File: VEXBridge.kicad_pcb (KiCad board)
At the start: 2 copper layers, 30 x 40 mm, 37 parts, among them J1 4P4C, J3 Conn_01x05_Pin, U1 LM2596S-5, U2 MAX481E, U5 SN74LVC2G14DBV

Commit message: VEXBridge v2 (WIP)
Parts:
- removed D4: ESDA5V3L, Package_TO_SOT_SMD:SOT-23-3
- removed U1: LM2596S-5, Package_TO_SOT_SMD:TO-263-5_TabPin3
- removed kibuzzard-675F6148: G***, kibuzzard-675F6148
- removed kibuzzard-675F61D9: G***, kibuzzard-675F61D9
- removed kibuzzard-675F61E2: G***, kibuzzard-675F61E2
- removed kibuzzard-675F61ED: G***, kibuzzard-675F61ED
- removed kibuzzard-675F6473: G***, kibuzzard-675F6473
- removed kibuzzard-675F648F: G***, kibuzzard-675F648F
- removed kibuzzard-675F6495: G***, kibuzzard-675F6495
- removed kibuzzard-676E54E7: G***, kibuzzard-676E54E7
- added C6: 10uF, Capacitor_SMD:C_0201_0603Metric, F.Cu at (81.0, 54.5)
- added C7: 22uF, Capacitor_SMD:C_1206_3216Metric, F.Cu at (81.0, 52.0)
- added C8: 1uF, Capacitor_SMD:C_0201_0603Metric, F.Cu at (63.3, 80.0)
- added F1: 1A, Fuse:Fuse_2010_5025Metric, F.Cu at (65.2, 43.0)
- added J10: QWIIC Connector, Connector_JST:JST_SH_SM04B-SRSS-TB_1x04-1MP_P1.00mm_Horizontal, F.Cu at (53.5, 37.5)
- added J2: Conn_01x04, Connector_Molex:Molex_PicoBlade_53047-0410_1x04_P1.25mm_Vertical, F.Cu at (91.3, 35.5)
- added J4: QWIIC Connector, Connector_JST:JST_SH_SM04B-SRSS-TB_1x04-1MP_P1.00mm_Horizontal, F.Cu at (53.5, 53.1)
- added J5: QWIIC Connector, Connector_JST:JST_SH_SM04B-SRSS-TB_1x04-1MP_P1.00mm_Horizontal, F.Cu at (53.5, 60.9)
- added J6: Conn_01x04, Connector_Molex:Molex_PicoBlade_53047-0410_1x04_P1.25mm_Vertical, F.Cu at (91.3, 51.0)
- added J7: Conn_01x04, Connector_Molex:Molex_PicoBlade_53047-0410_1x04_P1.25mm_Vertical, F.Cu at (91.3, 58.8)
- added J8: USB_C_Receptacle_USB2.0_14P, Connector_USB:USB_C_Plug_Molex_105444, F.Cu at (80.8, 26.6)
- added J9: QWIIC Connector, Connector_JST:JST_SH_SM04B-SRSS-TB_1x04-1MP_P1.00mm_Horizontal, F.Cu at (53.5, 45.3)
- added R10: 10k, Resistor_SMD:R_0805_2012Metric, F.Cu at (58.5, 39.0)
- added R11: 5.1k, Resistor_SMD:R_0805_2012Metric, F.Cu at (92.1, 76.2)
- added R13: 5.1k, Resistor_SMD:R_0805_2012Metric, F.Cu at (82.0, 30.5)
- added R14: 5.1k, Resistor_SMD:R_0805_2012Metric, F.Cu at (82.0, 32.5)
- added U3: LSM9DS1, Package_LGA:LGA-24L_3x3.5mm_P0.43mm, F.Cu at (58.4, 76.1)
- added U4: AMS1117-3.3, Package_TO_SOT_SMD:SOT-223-3_TabPin2, F.Cu at (81.0, 60.0)
- C1: value 100uF -> 220uF; footprint Capacitor_SMD:CP_Elec_6.3x7.7 -> Capacitor_SMD:C_1210_3225Metric
- C2: value 220uF -> 100uF; footprint Capacitor_SMD:CP_Elec_6.3x7.7 -> Capacitor_SMD:C_1206_3216Metric
- C3, C4: value 0.1uF -> 1uF; footprint Capacitor_SMD:C_0402_1005Metric -> Capacitor_SMD:C_0201_0603Metric
- D1: value LED -> RED
- D2: value LED -> GREEN
- D3: value LED -> D; footprint LED_SMD:LED_0603_1608Metric -> Diode_SMD:D_0201_0603Metric
- J3: value Conn_01x05_Pin -> Conn_01x04; footprint Connector_PinHeader_2.54mm:PinHeader_1x05_P2.54mm_Vertical -> Connector_Molex:Molex_PicoBlade_53047-0410_1x04_P1.25mm_Vertical
- L1: value 47uH -> 68uH; footprint Inductor_SMD:L_Coilcraft_LPS4018 -> Inductor_SMD:L_SXN_SMDRI127
- R1: value 100 -> 5.1k
- R2: value 120 -> 10k; footprint Resistor_SMD:R_1206_3216Metric -> Resistor_SMD:R_0805_2012Metric
- R3, R4: value 100 -> 10k
- U2: value MAX481E -> ESP32-S3-MINI-1U; footprint Package_SO:SOIC-8_3.9x4.9mm_P1.27mm -> RF_Module:ESP32-S2-MINI-1U
- U5: value SN74LVC2G14DBV -> LM2595S-5; footprint Package_TO_SOT_SMD:SOT-23-6 -> Package_TO_SOT_SMD:TO-263-5_TabPin3
- moved H1 83.5 mm to (55.0, 30.0)
- moved R6 73.0 mm to (58.5, 37.0), turned to 180 degrees
- moved H3 62.4 mm to (55.0, 85.0)
- moved D3 59.7 mm to (81.8, 34.5), turned to 180 degrees
- moved L1 56.9 mm to (32.0, 53.5)
- moved R5 56.2 mm to (58.5, 63.0)
- moved J1 54.8 mm to (70.3, 36.5), turned to 180 degrees
- moved R2 49.5 mm to (62.0, 81.5)
- moved C2 48.2 mm to (66.0, 47.0)
- moved R7 47.6 mm to (58.5, 45.0), turned to 180 degrees
- moved R3 47.4 mm to (58.5, 53.0), turned to 180 degrees
- moved C1 47.3 mm to (71.0, 47.0), turned to 180 degrees
- moved R8 44.8 mm to (58.5, 47.0), turned to 180 degrees
- moved R4 43.6 mm to (58.5, 61.0), turned to 180 degrees
- moved R9 38.5 mm to (58.5, 55.1), turned to 180 degrees
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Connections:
- C3 pad 1: +5V -> +3.3V
- C4 pad 1: +5V -> +3.3V
- D3 pad 1: GND -> +5V
- J1 pad 1: A -> unconnected-(J1-Pad1)
- J1 pad 2: B -> unconnected-(J1-Pad2)
- J1 pad 4: +12V -> Net-(F1-Pad1)
- J3 pad 1: RTS -> +5V
- J3 pad 2: RXD -> ENC_A1
- J3 pad 3: TXD -> ENC_B1
- R1 pad 1: +5V -> Net-(D1-A)
- R1 pad 2: Net-(D1-A) -> +3.3V
- R2 pad 1: B -> +3.3V
- R2 pad 2: A -> Net-(U2-EN)
- R3 pad 1: Net-(U5-1Y) -> +3.3V
- R3 pad 2: Net-(D2-A) -> SDA
- R4 pad 1: Net-(U5-2Y) -> +3.3V
- R4 pad 2: Net-(D3-A) -> SDA
- R5 pad 1: B -> +3.3V
- R5 pad 2: GND -> SCL
- R6 pad 1: +5V -> +3.3V
- R6 pad 2: A -> SDA
- R7 pad 1: +5V -> +3.3V
- R7 pad 2: TXD -> SDA
- R8 pad 1: RTS -> +3.3V
- R8 pad 2: GND -> SCL
- R9 pad 1: +5V -> +3.3V
- R9 pad 2: RXD -> SCL
- U2 pad 1: TXD -> GND
- U2 pad 2: RTS -> GND
- U2 pad 3: RTS -> +3.3V
- U2 pad 4: RXD -> SDA
- U2 pad 5: GND -> SCL
- U2 pad 6: A -> unconnected-(U2-IO2-Pad6)
- U2 pad 7: B -> unconnected-(U2-IO3-Pad7)
- U2 pad 8: +5V -> ENC_A1
- U5 pad 1: RXD -> Net-(D9-K)
- U5 pad 2: GND -> +12V
- U5 pad 3: TXD -> GND
- U5 pad 4: Net-(U5-2Y) -> +5V
- U5 pad 5: +5V -> GND
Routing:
- net +5V: track 91.8 -> 0.00 mm, vias 4 -> 0
- net GND: track 52.9 -> 0.00 mm, vias 7 -> 0
- net A: track 31.0 -> 0.00 mm, vias 2 -> 0
- net B: track 25.0 -> 0.00 mm
- net TXD: track 23.8 -> 0.00 mm, vias 3 -> 0
- net +12V: track 20.6 -> 0.00 mm
- net RXD: track 15.0 -> 0.00 mm, vias 1 -> 0
- net RTS: track 14.1 -> 0.00 mm, vias 1 -> 0
- net Net-(D9-K): track 12.2 -> 0.00 mm
- net Net-(U5-2Y): track 6.82 -> 0.00 mm
- net Net-(D2-A): track 4.65 -> 0.00 mm
- net Net-(D3-A): track 4.49 -> 0.00 mm
- net Net-(D1-A): track 4.34 -> 0.00 mm
- net Net-(U5-1Y): track 2.13 -> 0.00 mm
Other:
- board size 30 x 40 mm -> 45 x 65 mm

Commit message: Completed schematic
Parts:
- removed C1: 220uF, Capacitor_SMD:C_1210_3225Metric
- removed C2: 100uF, Capacitor_SMD:C_1206_3216Metric
- removed C3, C4, C8: 1uF, Capacitor_SMD:C_0201_0603Metric
- removed C6: 10uF, Capacitor_SMD:C_0201_0603Metric
- removed C7: 22uF, Capacitor_SMD:C_1206_3216Metric
- removed D1: RED, LED_SMD:LED_0603_1608Metric
- removed D2: GREEN, LED_SMD:LED_0603_1608Metric
- removed D3: D, Diode_SMD:D_0201_0603Metric
- removed D9: D_Schottky, Diode_SMD:D_SMA
- removed F1: 1A, Fuse:Fuse_2010_5025Metric
- removed G***: LOGO, LOGO
- removed H1, H2, H3, H4: MountingHole_Pad, MountingHole:MountingHole_2.7mm_M2.5_Pad
- removed J1: 4P4C, Connector_RJ:RJ9_Evercom_5301-440xxx_Horizontal
- removed J10, J4, J5, J9: QWIIC Connector, Connector_JST:JST_SH_SM04B-SRSS-TB_1x04-1MP_P1.00mm_Horizontal
- removed J2, J3, J6, J7: Conn_01x04, Connector_Molex:Molex_PicoBlade_53047-0410_1x04_P1.25mm_Vertical
- removed J8: USB_C_Receptacle_USB2.0_14P, Connector_USB:USB_C_Plug_Molex_105444
- removed L1: 68uH, Inductor_SMD:L_SXN_SMDRI127
- removed R1, R11, R13, R14: 5.1k, Resistor_SMD:R_0805_2012Metric
- removed R10, R2, R3, R4, R5, R6, R7, R8, R9: 10k, Resistor_SMD:R_0805_2012Metric
- removed U2: ESP32-S3-MINI-1U, RF_Module:ESP32-S2-MINI-1U
- removed U3: LSM9DS1, Package_LGA:LGA-24L_3x3.5mm_P0.43mm
- removed U4: AMS1117-3.3, Package_TO_SOT_SMD:SOT-223-3_TabPin2
- removed U5: LM2595S-5, Package_TO_SOT_SMD:TO-263-5_TabPin3
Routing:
- removed copper zone on B.Cu, net GND
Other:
- board outline removed

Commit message: Initial PCB Design w/o power rails
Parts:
- added C1: 0.1uF, Capacitor_SMD:C_0603_1608Metric, F.Cu at (131.3, 50.8)
- added C10: 1uF, Capacitor_SMD:C_0603_1608Metric, F.Cu at (131.2, 52.5)
- added C11: 1uF, Capacitor_SMD:C_0603_1608Metric, F.Cu at (104.0, 43.0)
- added C12: 4.7uF, Capacitor_SMD:C_0603_1608Metric, F.Cu at (80.5, 39.7)
- added C13: 1uF, Capacitor_SMD:C_0603_1608Metric, F.Cu at (117.0, 63.0)
- added C14: 22uF, Capacitor_SMD:C_0603_1608Metric, F.Cu at (79.0, 39.7)
- added C15: 1uF, Capacitor_SMD:C_0603_1608Metric, F.Cu at (99.0, 36.5)
- added C2: 10uF, Capacitor_SMD:C_0603_1608Metric, F.Cu at (120.5, 52.5)
- added C3: 220nF, Capacitor_SMD:C_0402_1005Metric, F.Cu at (119.0, 53.0)
- added C4: 22uF, Capacitor_SMD:C_0603_1608Metric, F.Cu at (136.5, 48.0)
- added C5: 22uF, Capacitor_SMD:C_0603_1608Metric, F.Cu at (136.5, 49.5)
- added C6: 22uF, Capacitor_SMD:C_0603_1608Metric, F.Cu at (136.5, 51.0)
- added C7: 22uF, Capacitor_SMD:C_0603_1608Metric, F.Cu at (136.5, 52.5)
- added C8: 10uF, Capacitor_SMD:C_0603_1608Metric, F.Cu at (139.3, 43.3)
- added C9: 22uF, Capacitor_SMD:C_0603_1608Metric, F.Cu at (139.3, 37.5)
- added D1: D, Diode_SMD:D_0201_0603Metric, F.Cu at (133.5, 47.5)
- added D2: D, Diode_SMD:D_0201_0603Metric, F.Cu at (136.5, 26.5)
- added D3: RED, LED_SMD:LED_0603_1608Metric, F.Cu at (93.0, 60.0)
- added D4: BLUE, LED_SMD:LED_0603_1608Metric, F.Cu at (86.5, 60.0)
- added F1: 2A, Fuse:Fuse_2010_5025Metric, F.Cu at (119.5, 57.5)
- added H1: MountingHole_Pad, MountingHole:MountingHole_2.7mm_M2.5_Pad, F.Cu at (137.5, 19.5)
- added H2: MountingHole_Pad, MountingHole:MountingHole_2.7mm_M2.5_Pad, F.Cu at (137.5, 71.0)
- added H3: MountingHole_Pad, MountingHole:MountingHole_2.7mm_M2.5_Pad, F.Cu at (42.0, 19.5)
- added H4: MountingHole_Pad, MountingHole:MountingHole_2.7mm_M2.5_Pad, F.Cu at (42.0, 71.0)
- added J1: VEX V5, Connector_RJ:RJ9_Evercom_5301-440xxx_Horizontal, F.Cu at (125.7, 63.6)
- added J10: Port 1, Connector_Molex:Molex_Mini-Fit_Jr_5569-04A2_2x02_P4.20mm_Horizontal, F.Cu at (53.5, 30.3)
- added J11: Port 2, Connector_Molex:Molex_Mini-Fit_Jr_5569-04A2_2x02_P4.20mm_Horizontal, F.Cu at (53.5, 41.7)
- added J12: Port 3, Connector_Molex:Molex_Mini-Fit_Jr_5569-04A2_2x02_P4.20mm_Horizontal, F.Cu at (53.5, 53.2)
- added J13: Port 4, Connector_Molex:Molex_Mini-Fit_Jr_5569-04A2_2x02_P4.20mm_Horizontal, F.Cu at (53.5, 64.7)
- added J14: USB_C_Receptacle_USB2.0_14P, Connector_USB:USB_C_Plug_Molex_105444, F.Cu at (139.0, 28.2)
- added J2: Port A, Connector_JST:JST_SH_SM04B-SRSS-TB_1x04-1MP_P1.00mm_Horizontal, F.Cu at (74.8, 70.1)
- added J3: Port B, Connector_JST:JST_SH_SM04B-SRSS-TB_1x04-1MP_P1.00mm_Horizontal, F.Cu at (83.3, 70.1)
- added J4: Port C, Connector_JST:JST_SH_SM04B-SRSS-TB_1x04-1MP_P1.00mm_Horizontal, F.Cu at (91.8, 70.1)
- added J5: Port D, Connector_JST:JST_SH_SM04B-SRSS-TB_1x04-1MP_P1.00mm_Horizontal, F.Cu at (100.3, 70.1)
- added J6: Port E, Connector_JST:JST_SH_SM04B-SRSS-TB_1x04-1MP_P1.00mm_Horizontal, F.Cu at (99.8, 20.4)
- added J7: Port F, Connector_JST:JST_SH_SM04B-SRSS-TB_1x04-1MP_P1.00mm_Horizontal, F.Cu at (91.3, 20.5)
- added J8: Port G, Connector_JST:JST_SH_SM04B-SRSS-TB_1x04-1MP_P1.00mm_Horizontal, F.Cu at (82.8, 20.5)
- added J9: Port H, Connector_JST:JST_SH_SM04B-SRSS-TB_1x04-1MP_P1.00mm_Horizontal, F.Cu at (74.3, 20.5)
- added JP2: Multiplexer Addr, Jumper:SolderJumper-3_P1.3mm_Bridged12_RoundedPad1.0x1.5mm, F.Cu at (101.0, 40.3)
- added L1: 10uH, Inductor_SMD:L_0603_1608Metric, F.Cu at (134.0, 50.3)
- added Q1: BSS138, Package_TO_SOT_SMD:SOT-23-3, F.Cu at (65.9, 31.0)
- added Q2: BSS138, Package_TO_SOT_SMD:SOT-23-3, F.Cu at (66.1, 42.0)
- added Q3: BSS138, Package_TO_SOT_SMD:SOT-23-3, F.Cu at (66.1, 53.5)
- added Q4: BSS138, Package_TO_SOT_SMD:SOT-23-3, F.Cu at (66.0, 65.4)
- added Q5: BSS138, Package_TO_SOT_SMD:SOT-23-3, F.Cu at (65.9, 26.0)
- added Q6: BSS138, Package_TO_SOT_SMD:SOT-23-3, F.Cu at (66.1, 37.0)
- added Q7: BSS138, Package_TO_SOT_SMD:SOT-23-3, F.Cu at (66.1, 48.5)
- added Q8: BSS138, Package_TO_SOT_SMD:SOT-23-3, F.Cu at (66.0, 59.5)
- added R1: 100k, Resistor_SMD:R_0805_2012Metric, F.Cu at (131.6, 54.5)
- added R10: 10k, Resistor_SMD:R_0805_2012Metric, F.Cu at (69.1, 42.0)
- added R11: 10k, Resistor_SMD:R_0805_2012Metric, F.Cu at (63.1, 40.5)
- added R12: 10k, Resistor_SMD:R_0805_2012Metric, F.Cu at (69.1, 53.5)
- added R13: 10k, Resistor_SMD:R_0805_2012Metric, F.Cu at (63.1, 52.0)
- added R14: 10k, Resistor_SMD:R_0805_2012Metric, F.Cu at (69.0, 65.6)
- added R15: 10k, Resistor_SMD:R_0805_2012Metric, F.Cu at (63.1, 63.5)
- added R16: 10k, Resistor_SMD:R_0805_2012Metric, F.Cu at (69.0, 26.0)
- added R17: 10k, Resistor_SMD:R_0805_2012Metric, F.Cu at (63.1, 27.5)
- added R18: 10k, Resistor_SMD:R_0805_2012Metric, F.Cu at (69.1, 36.9)
- added R19: 10k, Resistor_SMD:R_0805_2012Metric, F.Cu at (63.1, 38.5)
- added R2: 24k, Resistor_SMD:R_0805_2012Metric, F.Cu at (135.1, 54.5)
- added R20: 10k, Resistor_SMD:R_0805_2012Metric, F.Cu at (69.1, 48.5)
- added R21: 10k, Resistor_SMD:R_0805_2012Metric, F.Cu at (63.1, 50.0)
- added R22: 10k, Resistor_SMD:R_0805_2012Metric, F.Cu at (69.0, 59.5)
- added R23: 10k, Resistor_SMD:R_0805_2012Metric, F.Cu at (63.1, 61.5)
- added R24: 5.1k, Resistor_SMD:R_0805_2012Metric, F.Cu at (133.0, 25.5)
- added R25: 5.1k, Resistor_SMD:R_0805_2012Metric, F.Cu at (135.0, 25.5)
- added R26: 4.7k, Resistor_SMD:R_0805_2012Metric, F.Cu at (91.0, 59.8)
- added R27: 2.2k, Resistor_SMD:R_0805_2012Metric, F.Cu at (88.5, 59.8)
- added R28: 10k, Resistor_SMD:R_0805_2012Metric, F.Cu at (112.5, 70.5)
- added R29: 10k, Resistor_SMD:R_0805_2012Metric, F.Cu at (109.5, 66.5)
- added R3: 2k, Resistor_SMD:R_0805_2012Metric, F.Cu at (80.5, 54.6)
- added R30: 10k, Resistor_SMD:R_0805_2012Metric, F.Cu at (120.0, 68.5)
- added R31: 10k, Resistor_SMD:R_0805_2012Metric, F.Cu at (120.0, 64.5)
- added R32: 900, Resistor_SMD:R_0805_2012Metric, F.Cu at (138.6, 54.5)
- added R4: 2k, Resistor_SMD:R_0805_2012Metric, F.Cu at (78.5, 54.6)
- added R5: 10k, Resistor_SMD:R_0805_2012Metric, F.Cu at (99.4, 34.5)
- added R6: 10K, Resistor_SMD:R_0805_2012Metric, F.Cu at (104.0, 48.0)
- added R7: 10k, Resistor_SMD:R_0805_2012Metric, F.Cu at (113.0, 62.5)
- added R8: 10k, Resistor_SMD:R_0805_2012Metric, F.Cu at (69.0, 31.0)
- added R9: 10k, Resistor_SMD:R_0805_2012Metric, F.Cu at (63.1, 29.5)
- added SW1: Reset, Button_Switch_SMD:SW_SPST_TS-1088-xR020, F.Cu at (94.5, 34.0)
- added SW2: Boot, Button_Switch_SMD:SW_SPST_TS-1088-xR020, F.Cu at (85.0, 34.0)
- added U1: LMR33630ADDA, Package_SO:Texas_HSOP-8-1EP_3.9x4.9mm_P1.27mm_ThermalVias, F.Cu at (125.3, 52.6)
- added U2: AMS1117-3.3, Package_TO_SOT_SMD:SOT-223-3_TabPin2, F.Cu at (134.5, 40.4)
- added U3: D3V3XA4B10LP, Package_DFN_QFN:Diodes_UDFN-10_1x2.5mm_P0.5mm, F.Cu at (135.0, 30.6)
- added U4: PCA9548ADB, Package_SO:SSOP-24_5.3x8.2mm_P0.65mm, F.Cu at (109.4, 45.5)
- added U6: ESP32-S3-MINI-1U, RF_Module:ESP32-S2-MINI-1U, F.Cu at (89.7, 45.4)
- added U7: MAX485E, Package_SO:SOIC-8_3.9x4.9mm_P1.27mm, F.Cu at (115.0, 66.5)
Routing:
- net USB_D-: track 0.00 -> 60.0 mm, vias 0 -> 2
- net USB_D+: track 0.00 -> 58.6 mm, vias 0 -> 2
- net SCL8: track 0.00 -> 51.8 mm
- net SDA1: track 0.00 -> 47.9 mm
- net SCL7: track 0.00 -> 45.4 mm
- net SCL1: track 0.00 -> 44.4 mm
- net SDA8: track 0.00 -> 44.2 mm
- net SDA2: track 0.00 -> 41.4 mm
- net SCL6: track 0.00 -> 39.1 mm
- net TX: track 0.00 -> 38.9 mm, vias 0 -> 2
- net SDA7: track 0.00 -> 38.0 mm
- net SCL2: track 0.00 -> 37.8 mm
- net RTS: track 0.00 -> 35.2 mm, vias 0 -> 2
- net SDA3: track 0.00 -> 35.0 mm
- net SDA: track 0.00 -> 33.4 mm, vias 0 -> 2
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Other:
- board outline added: 103.5 x 59.5 mm

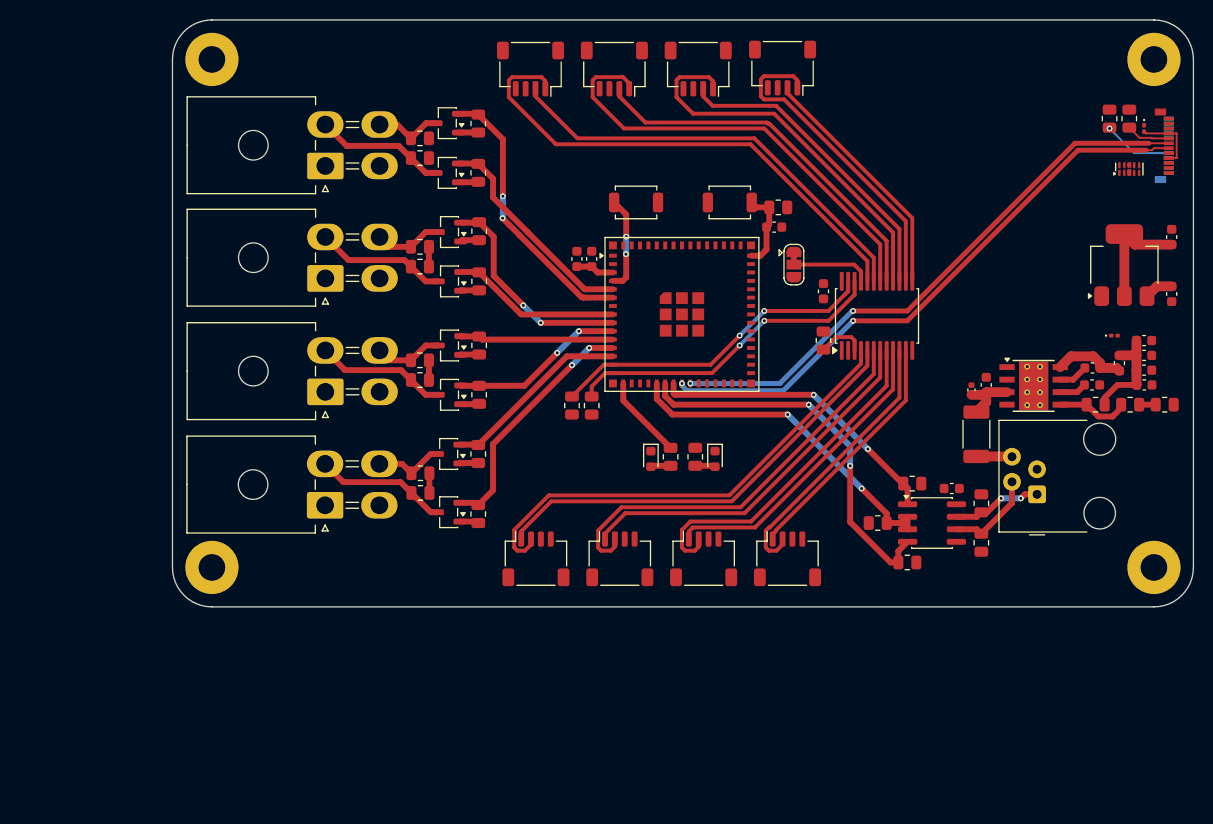
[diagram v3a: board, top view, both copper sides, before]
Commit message: (Mostly) complete PCB routing
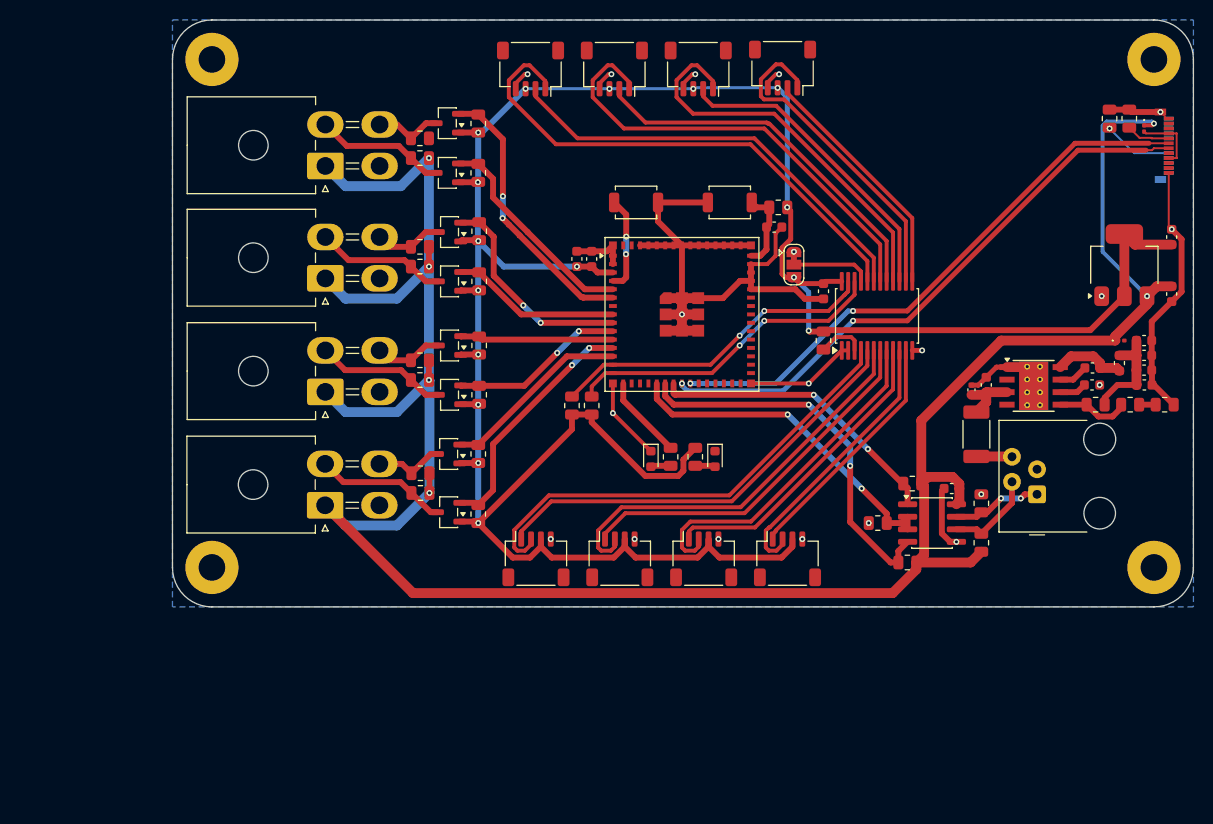
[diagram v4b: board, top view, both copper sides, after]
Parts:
- removed U3: D3V3XA4B10LP, Package_DFN_QFN:Diodes_UDFN-10_1x2.5mm_P0.5mm
- moved D1 0.84 mm to (134.2, 48.0)
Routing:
- net +5V: track 8.91 -> 242.0 mm, vias 0 -> 6
- net +3.3V: track 30.8 -> 252.9 mm, vias 0 -> 16
- net GND: track 0.00 -> 143.2 mm, vias 0 -> 20
- net SCL7: track 45.4 -> 46.5 mm
- net SCL5: track 32.5 -> 33.5 mm
- net SCL6: track 39.1 -> 40.1 mm
- net SCL8: track 51.8 -> 52.8 mm
- added copper zone on B.Cu, net GND

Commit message: Near-Final PCB Design
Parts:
- removed D1, D2: D, Diode_SMD:D_0201_0603Metric
- removed J14: USB_C_Receptacle_USB2.0_14P, Connector_USB:USB_C_Plug_Molex_105444
- removed U4: PCA9548ADB, Package_SO:SSOP-24_5.3x8.2mm_P0.65mm
- added G***: LOGO, LOGO, B.Cu at (114.0, 29.0)
- added J15: USB_C_Receptacle, Connector_USB:USB_C_Receptacle_Molex_105450-0101, F.Cu at (137.1, 29.0)
- added U3: D3V3XA4B10LP, Package_DFN_QFN:Diodes_UDFN-10_1x2.5mm_P0.5mm, F.Cu at (130.5, 26.9)
- added U5: TCA9548APWR, Package_SO:TSSOP-24_4.4x7.8mm_P0.65mm, F.Cu at (109.5, 46.0)
- added kibuzzard-69FA45C9: G***, kibuzzard-69FA45C9, F.Cu at (74.8, 74.0)
- added kibuzzard-69FA4619: G***, kibuzzard-69FA4619, F.Cu at (83.2, 74.0)
- added kibuzzard-69FA461D: G***, kibuzzard-69FA461D, F.Cu at (91.8, 74.0)
- added kibuzzard-69FA4621: G***, kibuzzard-69FA4621, F.Cu at (100.4, 74.0)
- added kibuzzard-69FA465C: G***, kibuzzard-69FA465C, F.Cu at (99.8, 16.4)
- added kibuzzard-69FA4660: G***, kibuzzard-69FA4660, F.Cu at (91.4, 16.4)
- added kibuzzard-69FA4664: G***, kibuzzard-69FA4664, F.Cu at (82.8, 16.4)
- added kibuzzard-69FA4669: G***, kibuzzard-69FA4669, F.Cu at (74.4, 16.4)
- added kibuzzard-69FA46AE: G***, kibuzzard-69FA46AE, F.Cu at (38.6, 28.0)
- added kibuzzard-69FA46BE: G***, kibuzzard-69FA46BE, F.Cu at (38.6, 62.6)
- added kibuzzard-69FA46C2: G***, kibuzzard-69FA46C2, F.Cu at (38.6, 51.2)
- added kibuzzard-69FA46C9: G***, kibuzzard-69FA46C9, F.Cu at (38.6, 39.6)
- C14, C4, C5, C6, C7, C9: footprint Capacitor_SMD:C_0603_1608Metric -> Capacitor_SMD:C_0805_2012Metric
- D4: value BLUE -> GREEN
- F1: footprint Fuse:Fuse_2010_5025Metric -> Fuse:Fuse_1812_4532Metric
- L1: footprint Inductor_SMD:L_0603_1608Metric -> Inductor_SMD:L_TechFuse_SL0420
- R26: value 4.7k -> 330
- R27: value 2.2k -> 150
- R32: value 900 -> 820; footprint Resistor_SMD:R_0805_2012Metric -> Resistor_SMD:R_0603_1608Metric
- moved C4 8.93 mm to (138.5, 39.3)
- moved C5 8.44 mm to (138.5, 41.3)
- moved C6 7.96 mm to (138.5, 43.3)
- moved C7 7.45 mm to (138.4, 45.3)
- moved R25 5.85 mm to (129.5, 23.5)
- moved C8 5.31 mm to (134.3, 45.1)
- moved C9 5.31 mm to (134.3, 39.3)
- moved U2 5.31 mm to (129.5, 42.1)
- moved R24 2.50 mm to (131.5, 23.5)
- moved J1 2.00 mm to (127.7, 63.5)
- moved L1 1.51 mm to (135.5, 50.5)
- moved H3 0.60 mm to (41.4, 19.5)
- moved H4 0.60 mm to (41.4, 71.0)
- moved C14 0.50 mm to (78.5, 39.7)
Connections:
- C4 pad 1: Net-(D1-A) -> +5V
- C5 pad 1: Net-(D1-A) -> +5V
- C6 pad 1: Net-(D1-A) -> +5V
- C7 pad 1: Net-(D1-A) -> +5V
- L1 pad 2: Net-(D1-A) -> +5V
- R1 pad 1: Net-(D1-A) -> +5V
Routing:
- net SCL6: track 40.1 -> 28.6 mm
- net SCL7: track 46.5 -> 35.5 mm
- net Net-(D1-A): track 10.8 -> 0.00 mm
- net SCL8: track 52.8 -> 42.5 mm
- net SCL5: track 33.5 -> 25.3 mm
- net Net-(J15-CC1): track 4.45 -> 11.3 mm, vias 0 -> 2
- net Net-(D2-A): track 6.67 -> 0.00 mm
- net GND: track 143.2 -> 148.9 mm, vias 20 -> 22
- net +5V: track 242.0 -> 237.1 mm
- net SDA5: track 24.9 -> 29.0 mm
- net +3.3V: track 252.9 -> 250.8 mm
- net Net-(F1-Pad1): track 3.62 -> 5.68 mm
- net B: track 9.12 -> 11.2 mm
- net Net-(U1-SW): track 7.34 -> 9.34 mm
- net SDA8: track 44.2 -> 45.9 mm
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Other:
- board size 103.5 x 59.5 mm -> 104.1 x 59.5 mm
- board text added: "JLCJLCJLCJLC"

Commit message: Fixed USB-C via diameters
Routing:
- net Net-(J15-CC2): track 5.73 -> 5.18 mm
